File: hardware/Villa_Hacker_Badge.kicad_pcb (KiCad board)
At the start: 2 copper layers, 45.1 x 50 mm, 24 parts, among them J1 Conn_02x03_Odd_Even, SW1 SW_RST, SW2 On, U1 PY32F002AA15M6TU

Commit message: fix(hw): logo EC
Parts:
- added kibuzzard-6685D235: G***, kibuzzard-6685D235, B.Cu at (71.7, 68.4)
- moved kibuzzard-668588B5 4.70 mm to (71.8, 70.8)
- moved G*** 3.08 mm to (69.6, 60.1)

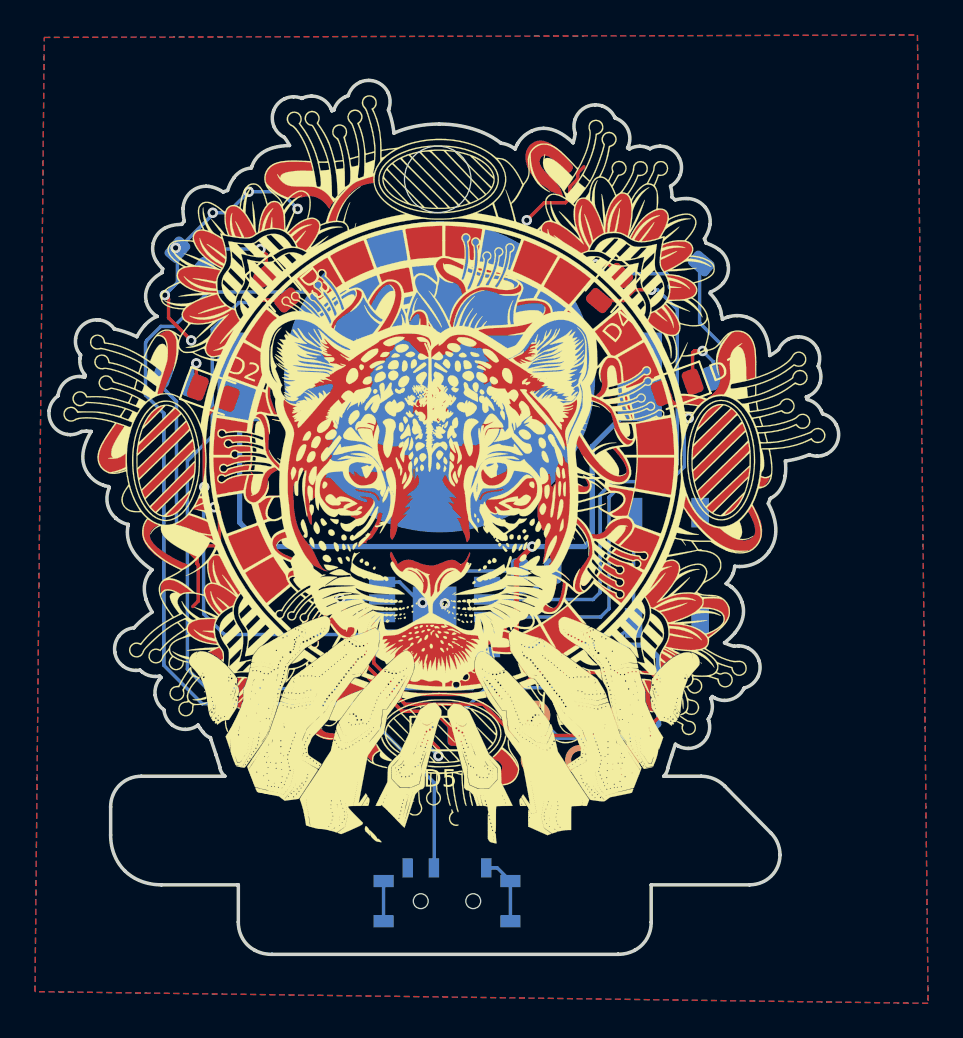
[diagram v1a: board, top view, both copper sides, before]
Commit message: feat(hw): remove zones
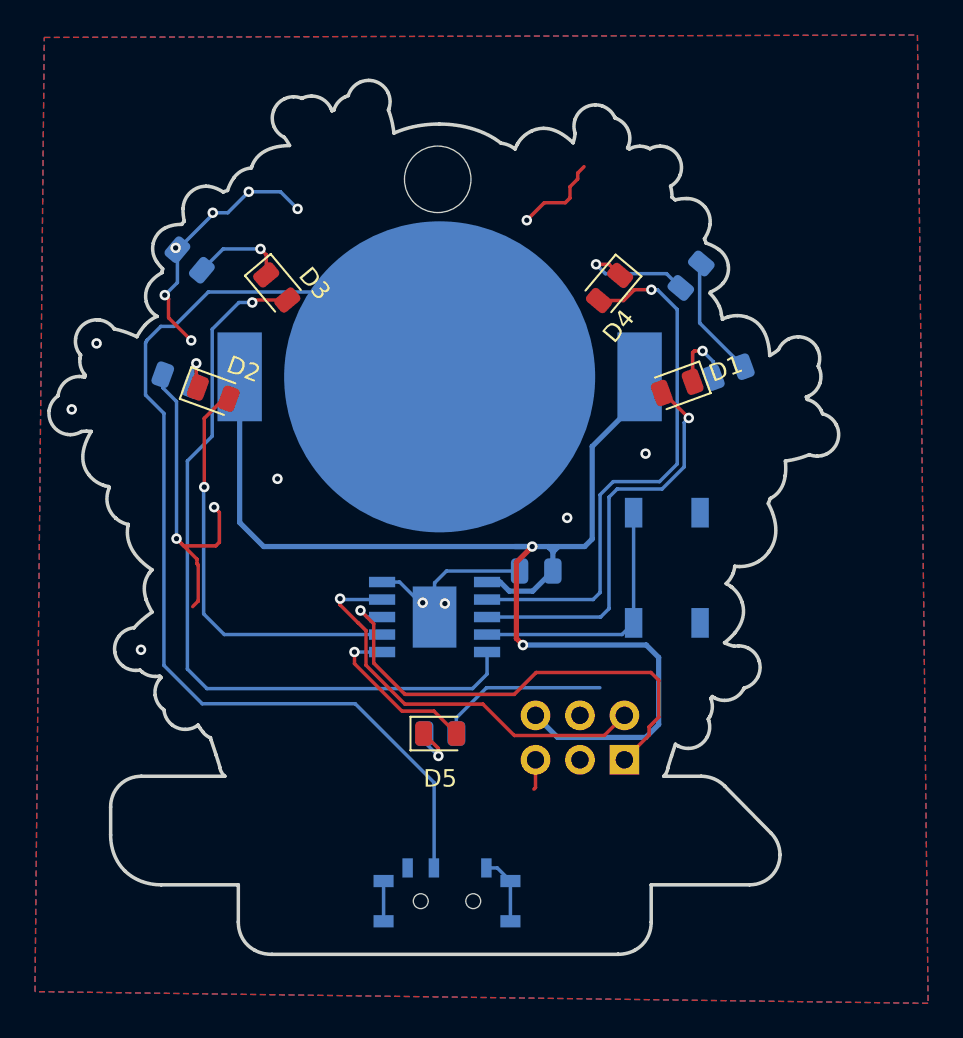
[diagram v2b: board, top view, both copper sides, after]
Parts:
- removed Ref**: Val**, Villa:Archivo SVG Badge La villa Hacker
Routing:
- net GND: vias 11 -> 17
- removed copper zone on F.Cu, net +3.3V
